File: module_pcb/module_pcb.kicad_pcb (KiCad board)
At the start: 2 copper layers, 247.5 x 25 mm, 106 parts, among them J1 ISP, J2 US, J3 DS, Q1 HSS2307, Q2 BSS123, U1 W25Q16JV, U2 AP1117-33, U3 TPS563200, U5 ATmega328P-AU, U7 74LVC1G34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

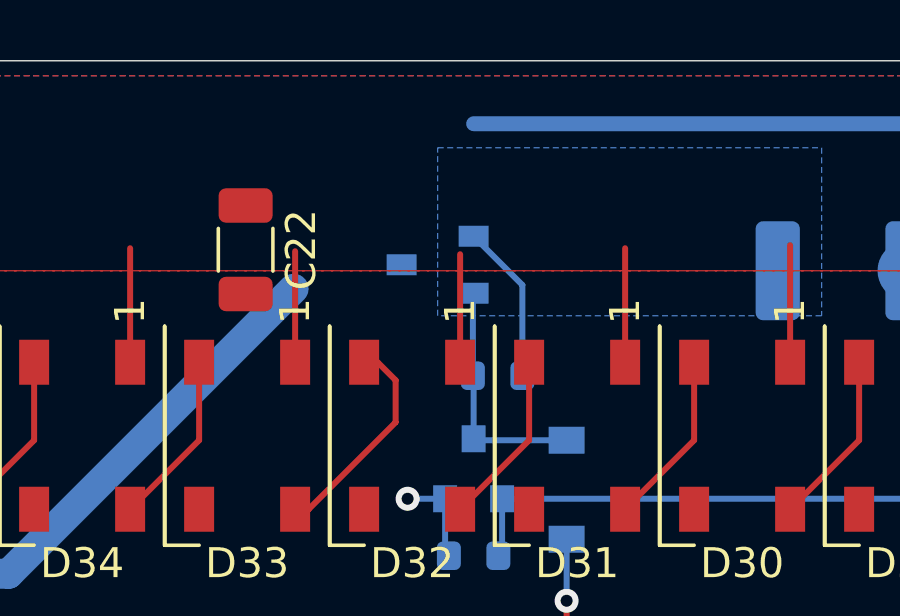
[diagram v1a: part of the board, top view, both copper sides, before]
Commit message: Fixed wrong pinout of p-channel mosfet for power control on main pcb and module pcb
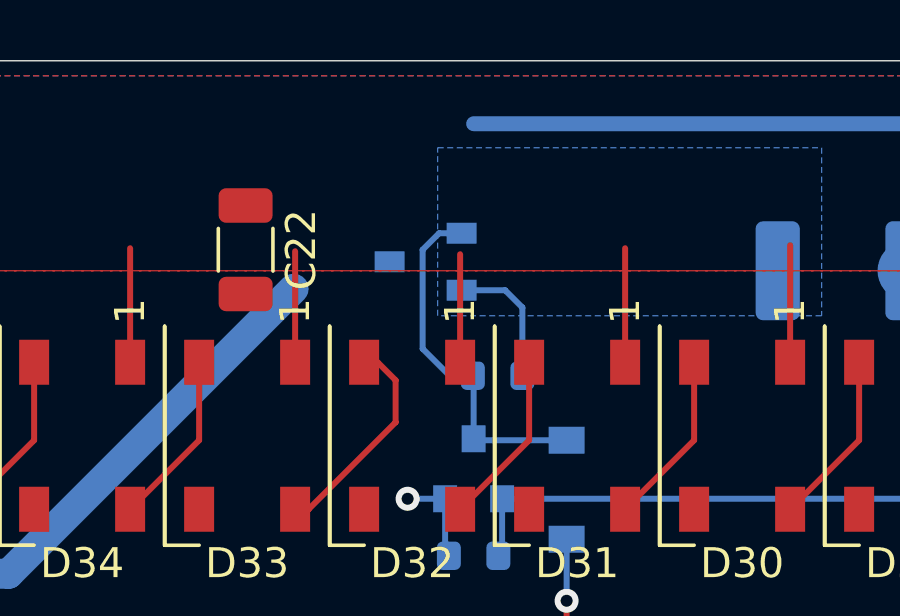
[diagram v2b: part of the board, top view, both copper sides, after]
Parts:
- moved Q1 0.41 mm to (94.7, 106.7)
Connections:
- Q1 pad 1: /BAT_RAW -> Net-(D47-Pad2)
- Q1 pad 2: Net-(D47-Pad2) -> /BAT_RAW
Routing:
- net Net-(D47-Pad2): track 7.99 -> 12.1 mm
- net /BAT_RAW: track 5.32 -> 4.54 mm
